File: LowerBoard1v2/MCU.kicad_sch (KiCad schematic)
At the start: 113 parts, among them J401 PWR, J402 DATA, J403 SWD Header, J404 MIDI_In, J405 Micro_SD_Card_Det2, J406 MIDI_Out, J407 MIDI_Thru, J408 POWER, SW401 RST, SW402 BOOT, U401 STM32F411RETx, U402 TPS56528DDA, U404 74HC04, U405 6N138, Y401 16MHz, Y402 32.768kHZ

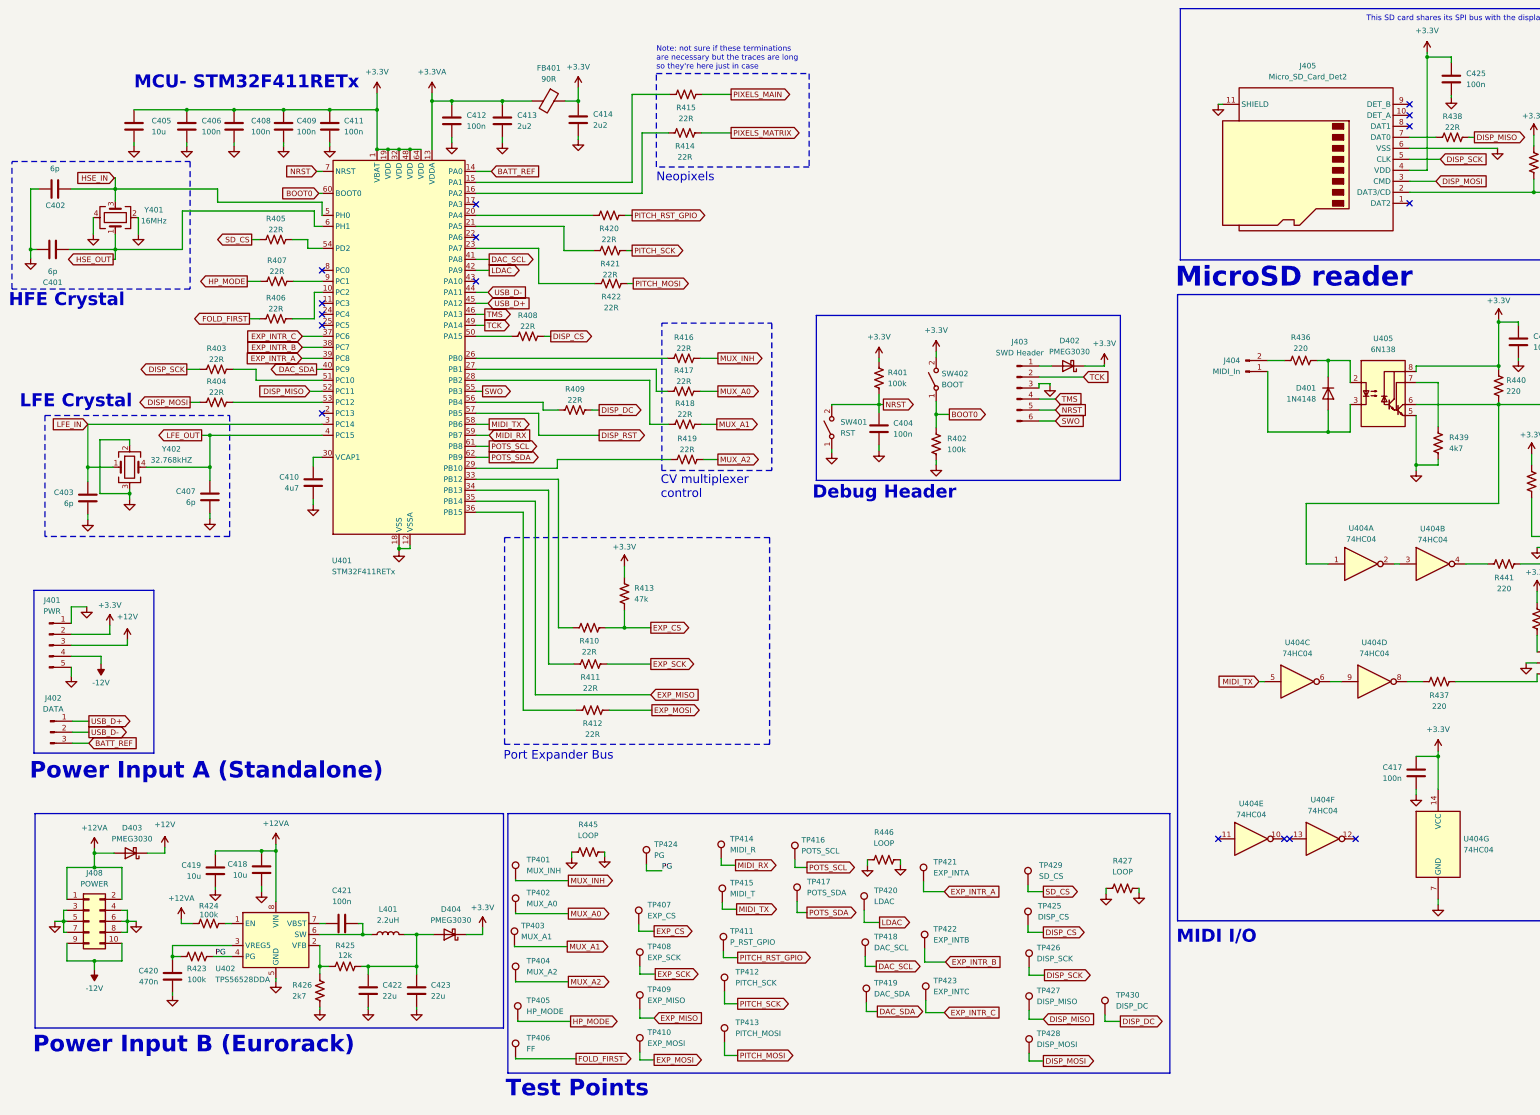
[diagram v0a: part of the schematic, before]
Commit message: switched to resistor arrays for schematic
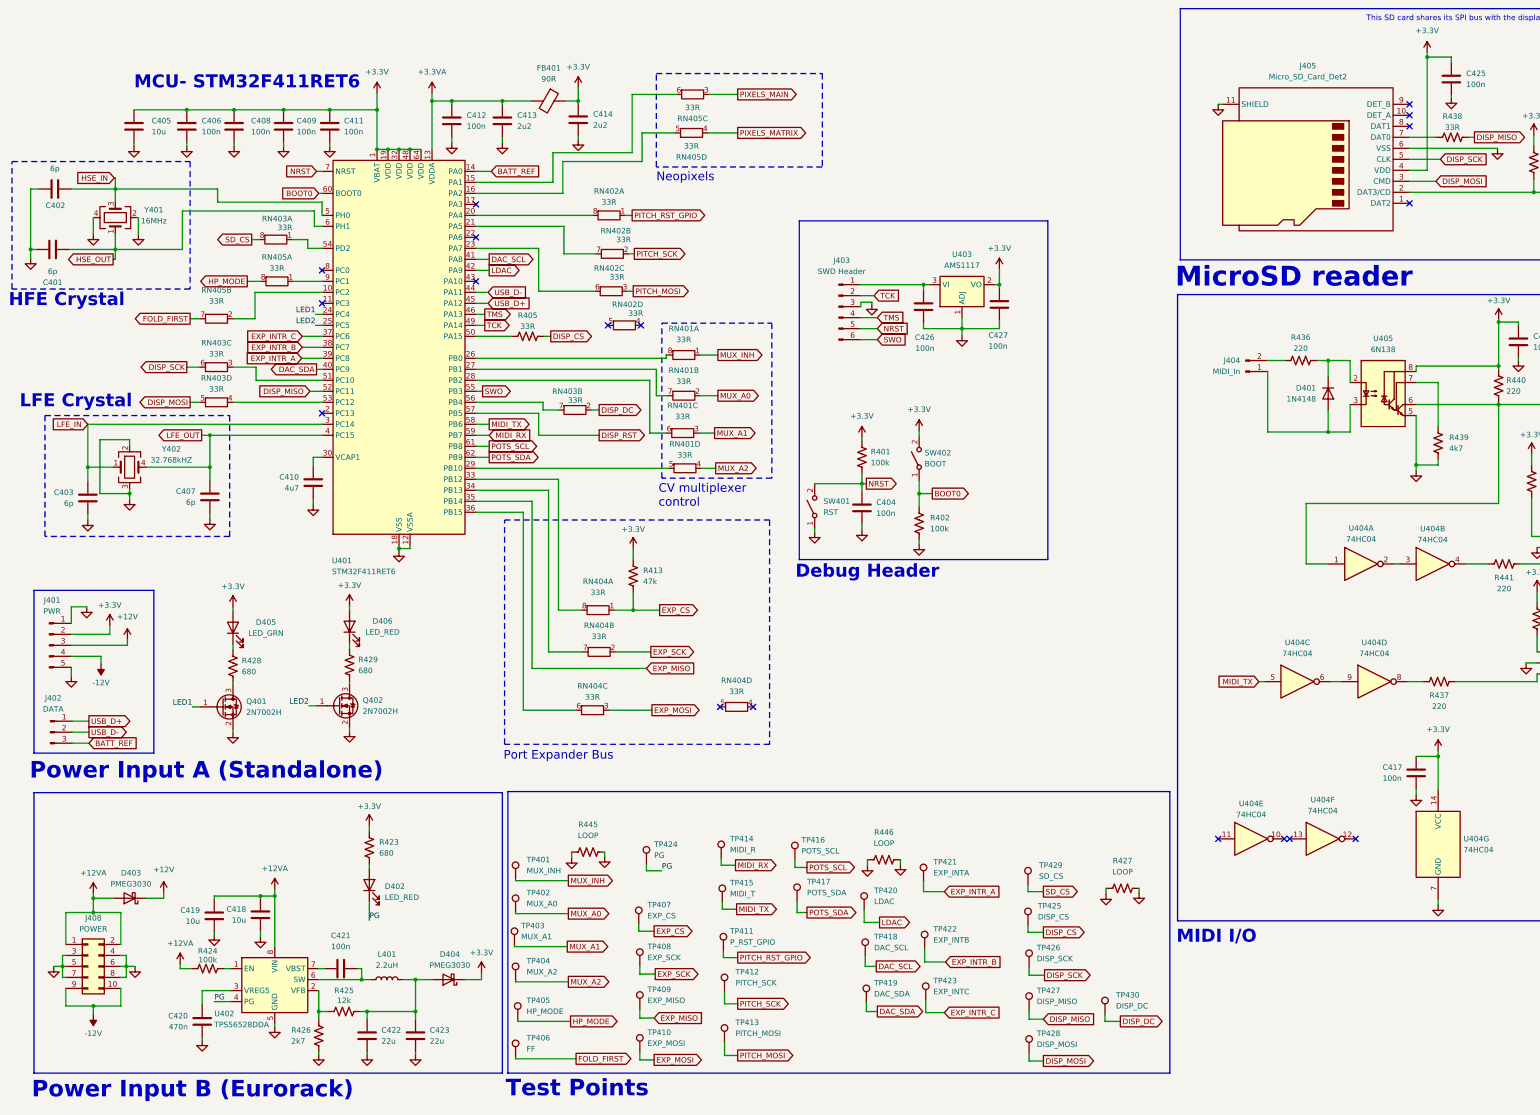
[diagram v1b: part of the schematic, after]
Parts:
- removed D402: PMEG3030, Diode_SMD:D_SOD-123, symbol Device:D_Schottky
- removed R403, R404, R406, R407, R408, R409, R410, R411, R412, R414, R415, R416, R417, R418, R419, R420, R421, R422: 22R, Resistor_SMD:R_0805_2012Metric, symbol Device:R_US
- added C426, C427: 100n, Capacitor_SMD:C_0805_2012Metric, symbol Device:C
- added D402: LED_RED, LED_SMD:LED_0805_2012Metric, symbol Device:LED
- added D405: LED_GRN, LED_THT:LED_D3.0mm, symbol Device:LED
- added D406: LED_RED, LED_THT:LED_D3.0mm, symbol Device:LED
- added Q401, Q402: 2N7002H, Package_TO_SOT_SMD:SOT-23, symbol Transistor_FET:2N7002H
- added R428, R429: 680, Resistor_SMD:R_0805_2012Metric, symbol Device:R_US
- added RN401, RN402, RN403, RN404, RN405: 33R, Resistor_SMD:R_Array_Concave_4x0603, symbol Device:R_Pack04_Split
- added U403: AMS1117, Package_TO_SOT_SMD:SOT-223-3_TabPin2, symbol Regulator_Linear:AMS1117
- R405, R438: value 22R -> 33R
- R423: value 100k -> 680
- U401: value STM32F411RETx -> STM32F411RET6
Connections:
- net +3.3V: now also R423.1, C427.2, D405.2 (A), D406.2 (A), U403.2 (VO)
- net DISP_CS: now also R405.2
- net DISP_DC: now also RN403.2 (R2.1)
- net DISP_MOSI: now also RN403.5 (R4.2)
- net DISP_SCK: now also RN403.6 (R3.2)
- net EXP_CS: now also RN404.1 (R1.1)
- net EXP_MOSI: now also RN404.3 (R3.1)
- net EXP_SCK: now also RN404.2 (R2.1)
- net FOLD_FIRST: now also RN405.7 (R2.2)
- net GND: now also C426.1, C427.1, Q401.2 (S), Q402.2 (S), U403.1 (ADJ)
- net HP_MODE: now also RN405.8 (R1.2)
- net MUX_A0: now also RN401.2 (R2.1)
- net MUX_A1: now also RN401.3 (R3.1)
- net MUX_A2: now also RN401.4 (R4.1)
- net MUX_INH: now also RN401.1 (R1.1)
- net PG: now also D402.1 (K); no longer R423.2
- net PITCH_MOSI: now also RN402.3 (R3.1)
- net PITCH_RST_GPIO: now also RN402.1 (R1.1)
- net PITCH_SCK: now also RN402.2 (R2.1)
- net PIXELS_MAIN: now also RN405.3 (R3.1)
- net PIXELS_MATRIX: now also RN405.4 (R4.1)
- net SD_CS: now also RN403.8 (R1.2); no longer R405.1
- net at U401.34 (PB13): now also RN404.7 (R2.2)
- net at U401.23 (PA7): now also RN402.6 (R3.2)
- net at U401.10 (PC2): now also RN405.2 (R2.1)
- net at U401.36 (PB15): now also RN404.6 (R3.2)
- net at J403.1 (Pin_1): now also C426.2, U403.3 (VI)
- net at U401.15 (PA1): now also RN405.6 (R3.2)
- net at U401.16 (PA2): now also RN405.5 (R4.2)
- net at U401.20 (PA4): now also RN402.8 (R1.2)
- net at U401.21 (PA5): now also RN402.7 (R2.2)
- net LED1: now reaches U401.24 (PC4)
- net LED1: now also Q401.1 (G)
- net LED2: now reaches U401.25 (PC5)
- net LED2: now also Q402.1 (G)
- net at U401.26 (PB0): now also RN401.8 (R1.2)
- net at U401.27 (PB1): now also RN401.7 (R2.2)
- net at U401.28 (PB2): now also RN401.6 (R3.2)
- net at U401.29 (PB10): now also RN401.5 (R4.2)
- net at U401.33 (PB12): now also RN404.8 (R1.2)
- net at U401.50 (PA15): now also R405.1
- net at U401.51 (PC10): now also RN403.3 (R3.1)
- net at U401.53 (PC12): now also RN403.4 (R4.1)
- net at U401.54 (PD2): now also RN403.1 (R1.1); no longer R405.2
- net at U401.56 (PB4): now also RN403.7 (R2.2)
- net at U401.9 (PC1): now also RN405.1 (R1.1)
- net at C420.1, U402.3 (VREG5): no longer R423.1
- new net: Q402.3 (D), R429.2
- new net: D406.1 (K), R429.1
- new net: D402.2 (A), R423.2
- new net: D405.1 (K), R428.1
- new net: Q401.3 (D), R428.2
- no-connect marks 16 -> 18
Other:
- note added: "MCU- STM32F411RET6"
- note removed: "MCU- STM32F411RETx"
- note removed: "Note: not sure if these terminations are necessary but the traces are long so they're here just in case"
- moved on the sheet: C404, C418, C419, C420, C421, C422, C423, D403, D404, J403, J408, L401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

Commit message: 1v2 layout
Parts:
- D405, D406: footprint LED_THT:LED_D3.0mm -> LED_SMD:LED_0805_2012Metric
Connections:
- net DISP_DC: now also RN403.8 (R1.2); no longer RN403.2 (R2.1)
- net DISP_MOSI: now also RN403.6 (R3.2); no longer RN403.5 (R4.2)
- net DISP_SCK: now also RN403.5 (R4.2); no longer RN403.6 (R3.2)
- net FOLD_FIRST: now also RN405.2 (R2.1); no longer RN405.7 (R2.2)
- net HP_MODE: now also RN405.1 (R1.1); no longer RN405.8 (R1.2)
- net SD_CS: now also RN403.7 (R2.2); no longer RN403.8 (R1.2)
- net at RN403.1 (R1.1): now also U401.56 (PB4); no longer U401.54 (PD2)
- net at U401.10 (PC2): now also RN405.7 (R2.2); no longer RN405.2 (R2.1)
- net at U401.51 (PC10): now also RN403.4 (R4.1); no longer RN403.3 (R3.1)
- net at U401.53 (PC12): now also RN403.3 (R3.1); no longer RN403.4 (R4.1)
- net at U401.9 (PC1): now also RN405.8 (R1.2); no longer RN405.1 (R1.1)
- new net: RN403.2 (R2.1), U401.54 (PD2)
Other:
- moved on the sheet: RN403A, RN403B, RN403C, RN403D, RN405A, RN405B
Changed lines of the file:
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@@
 		(exclude_from_sim no)
 		(in_bom no)
-		(on_board yes)
+		(on_board no)
 		(dnp no)
 		(fields_autoplaced yes)
@@
 		(exclude_from_sim no)
 		(in_bom no)
-		(on_board yes)
+		(on_board no)
 		(dnp no)
 		(fields_autoplaced yes)
@@
 		(exclude_from_sim no)
 		(in_bom no)
-		(on_board yes)
+		(on_board no)
 		(dnp no)
 		(fields_autoplaced yes)
@@
 	(symbol
 		(lib_id "Device:R_Pack04_Split")
-		(at 81.534 68.326 90)
+		(at 150.622 107.696 270)
+		(mirror x)
 		(unit 1)
 		(exclude_from_sim no)
@@
 		(dnp no)
 		(property "Reference" "RN403"
-			(at 85.344 64.262 90)
+			(at 146.812 103.632 90)
 			(effects
 				(font
@@
 		)
 		(property "Value" "33R"
-			(at 85.344 66.294 90)
+			(at 146.812 105.664 90)
 			(effects
 				(font
@@
 		)
 		(property "Footprint" "Resistor_SMD:R_Array_Concave_4x0603"
-			(at 81.534 70.358 90)
+			(at 150.622 109.728 90)
 			(effects
 				(font
@@
 		)
 		(property "Datasheet" "~"
-			(at 81.534 68.326 0)
+			(at 150.622 107.696 0)
 			(effects
 				(font
@@
 		)
 		(property "Description" "4 resistor network, parallel topology, split"
-			(at 81.534 68.326 0)
+			(at 150.622 107.696 0)
 			(effects
 				(font
@@
 		(exclude_from_sim no)
 		(in_bom no)
-		(on_board yes)
+		(on_board no)
 		(dnp no)
 		(fields_autoplaced yes)
@@
 		(exclude_from_sim no)
 		(in_bom no)
-		(on_board yes)
+		(on_board no)
 		(dnp no)
 		(fields_autoplaced yes)
@@
 		(exclude_from_sim no)
 		(in_bom no)
-		(on_board yes)
+		(on_board no)
 		(dnp no)
 		(fields_autoplaced yes)
@@
 		(exclude_from_sim no)
 		(in_bom no)
-		(on_board yes)
+		(on_board no)
 		(dnp no)
 		(fields_autoplaced yes)
@@
 		(exclude_from_sim no)
 		(in_bom no)
-		(on_board yes)
+		(on_board no)
 		(dnp no)
 		(fields_autoplaced yes)
@@
 	(symbol
 		(lib_id "Device:R_Pack04_Split")
-		(at 150.622 107.696 90)
+		(at 81.534 68.326 90)
 		(unit 2)
 		(exclude_from_sim no)
@@
 		(dnp no)
 		(property "Reference" "RN403"
-			(at 152.4 104.14 90)
+			(at 83.312 64.77 90)
 			(effects
 				(font
@@
 		)
 		(property "Value" "33R"
-			(at 152.4 106.172 90)
+			(at 83.312 66.802 90)
 			(effects
 				(font
@@
 		)
 		(property "Footprint" "Resistor_SMD:R_Array_Concave_4x0603"
-			(at 150.622 109.728 90)
+			(at 81.534 70.358 90)
 			(effects
 				(font
@@
 		)
 		(property "Datasheet" "~"
-			(at 150.622 107.696 0)
+			(at 81.534 68.326 0)
 			(effects
 				(font
@@
 		)
 		(property "Description" "4 resistor network, parallel topology, split"
-			(at 150.622 107.696 0)
+			(at 81.534 68.326 0)
 			(effects
 				(font
@@
 		(exclude_from_sim no)
 		(in_bom no)
-		(on_board yes)
+		(on_board no)
 		(dnp no)
 		(fields_autoplaced yes)
@@
 		(exclude_from_sim no)
 		(in_bom no)
-		(on_board yes)
+		(on_board no)
 		(dnp no)
 		(fields_autoplaced yes)
@@
 		(exclude_from_sim no)
 		(in_bom no)
-		(on_board yes)
+		(on_board no)
 		(dnp no)
 		(fields_autoplaced yes)
@@
 		(exclude_from_sim no)
 		(in_bom no)
-		(on_board yes)
+		(on_board no)
 		(dnp no)
 		(fields_autoplaced yes)
@@
 		(exclude_from_sim no)
 		(in_bom no)
-		(on_board yes)
+		(on_board no)
 		(dnp no)
 		(fields_autoplaced yes)
@@
 		(exclude_from_sim no)
 		(in_bom no)
-		(on_board yes)
+		(on_board no)
 		(dnp no)
 		(fields_autoplaced yes)
@@
 	(symbol
 		(lib_id "Device:R_Pack04_Split")
-		(at 67.818 105.918 90)
+		(at 67.818 97.79 90)
 		(unit 4)
 		(exclude_from_sim no)
@@
 		(fields_autoplaced yes)
 		(property "Reference" "RN403"
-			(at 67.818 100.33 90)
+			(at 67.818 92.202 90)
 			(effects
 				(font
@@
 		)
 		(property "Value" "33R"
-			(at 67.818 102.87 90)
+			(at 67.818 94.742 90)
 			(effects
 				(font
@@
 		)
 		(property "Footprint" "Resistor_SMD:R_Array_Concave_4x0603"
-			(at 67.818 107.95 90)
+			(at 67.818 99.822 90)
 			(effects
 				(font
@@
 		)
 		(property "Datasheet" "~"
-			(at 67.818 105.918 0)
+			(at 67.818 97.79 0)
 			(effects
 				(font
@@
 		)
 		(property "Description" "4 resistor network, parallel topology, split"
-			(at 67.818 105.918 0)
+			(at 67.818 97.79 0)
 			(effects
 				(font
@@
 		(exclude_from_sim no)
 		(in_bom no)
-		(on_board yes)
+		(on_board no)
 		(dnp no)
 		(fields_autoplaced yes)
@@
 		(exclude_from_sim no)
 		(in_bom no)
-		(on_board yes)
+		(on_board no)
 		(dnp no)
 		(fields_autoplaced yes)
@@
 		(exclude_from_sim no)
 		(in_bom no)
-		(on_board yes)
+		(on_board no)
 		(dnp no)
 		(fields_autoplaced yes)
@@
 	(symbol
 		(lib_id "Device:R_Pack04_Split")
-		(at 67.818 97.79 90)
+		(at 67.818 105.918 90)
 		(unit 3)
 		(exclude_from_sim no)
@@
 		(fields_autoplaced yes)
 		(property "Reference" "RN403"
-			(at 67.818 92.202 90)
+			(at 67.818 100.33 90)
 			(effects
 				(font
@@
 		)
 		(property "Value" "33R"
-			(at 67.818 94.742 90)
+			(at 67.818 102.87 90)
 			(effects
 				(font
@@
 		)
 		(property "Footprint" "Resistor_SMD:R_Array_Concave_4x0603"
-			(at 67.818 99.822 90)
+			(at 67.818 107.95 90)
 			(effects
 				(font
@@
 		)
 		(property "Datasheet" "~"
-			(at 67.818 97.79 0)
+			(at 67.818 105.918 0)
 			(effects
 				(font
@@
 		)
 		(property "Description" "4 resistor network, parallel topology, split"
-			(at 67.818 97.79 0)
+			(at 67.818 105.918 0)
 			(effects
 				(font
@@
 		(exclude_from_sim no)
 		(in_bom no)
-		(on_board yes)
+		(on_board no)
 		(dnp no)
 		(fields_autoplaced yes)
@@
 		(exclude_from_sim no)
 		(in_bom no)
-		(on_board yes)
+		(on_board no)
 		(dnp no)
 		(fields_autoplaced yes)
@@
 		(exclude_from_sim no)
 		(in_bom no)
-		(on_board yes)
+		(on_board no)
 		(dnp no)
 		(fields_autoplaced yes)
@@
 		(exclude_from_sim no)
 		(in_bom no)
-		(on_board yes)
+		(on_board no)
 		(dnp no)
 		(fields_autoplaced yes)
@@
 	(symbol
 		(lib_id "Device:R_Pack04_Split")
-		(at 81.788 77.978 90)
+		(at 81.788 77.978 270)
+		(mirror x)
 		(unit 1)
 		(exclude_from_sim no)
@@
 		(on_board yes)
 		(dnp no)
-		(fields_autoplaced yes)
 		(property "Reference" "RN405"
 			(at 81.788 72.39 90)
@@
 		(exclude_from_sim no)
 		(in_bom no)
-		(on_board yes)
+		(on_board no)
 		(dnp no)
 		(fields_autoplaced yes)
@@
 		(exclude_from_sim no)
 		(in_bom no)
-		(on_board yes)
+		(on_board no)
 		(dnp no)
 		(fields_autoplaced yes)
@@
 	(symbol
 		(lib_id "Device:R_Pack04_Split")
-		(at 67.818 86.614 90)
+		(at 67.818 86.614 270)
+		(mirror x)
 		(unit 2)
 		(exclude_from_sim no)
@@
 		(on_board yes)
 		(dnp no)
-		(fields_autoplaced yes)
 		(property "Reference" "RN405"
-			(at 67.818 80.01 90)
+			(at 67.818 81.026 90)
 			(effects
 				(font
@@
 		)
 		(property "Value" "33R"
-			(at 67.818 82.55 90)
+			(at 67.818 83.566 90)
 			(effects
 				(font
@@
 		(exclude_from_sim no)
 		(in_bom no)
-		(on_board yes)
+		(on_board no)
 		(dnp no)
 		(fields_autoplaced yes)
@@
 			)
 		)
-		(property "Footprint" "LED_THT:LED_D3.0mm"
+		(property "Footprint" "LED_SMD:LED_0805_2012Metric"
 			(at 71.628 157.988 0)
 			(effects
@@
 		(exclude_from_sim no)
 		(in_bom no)
-		(on_board yes)
+		(on_board no)
 		(dnp no)
 		(fields_autoplaced yes)
@@
 		(exclude_from_sim no)
 		(in_bom no)
-		(on_board yes)
+		(on_board no)
 		(dnp no)
 		(fields_autoplaced yes)
@@
 		(exclude_from_sim no)
 		(in_bom no)
-		(on_board yes)
+		(on_board no)
 		(dnp no)
 		(fields_autoplaced yes)
@@
 		(exclude_from_sim no)
 		(in_bom no)
-		(on_board yes)
+		(on_board no)
 		(dnp no)
 		(fields_autoplaced yes)
@@
 			)
 		)
-		(property "Footprint" "LED_THT:LED_D3.0mm"
+		(property "Footprint" "LED_SMD:LED_0805_2012Metric"
 			(at 98.552 157.734 0)
 			(effects
@@
 		(exclude_from_sim no)
 		(in_bom no)
-		(on_board yes)
+		(on_board no)
 		(dnp no)
 		(fields_autoplaced yes)
@@
 		(exclude_from_sim no)
 		(in_bom no)
-		(on_board yes)
+		(on_board no)
 		(dnp no)
 		(fields_autoplaced yes)

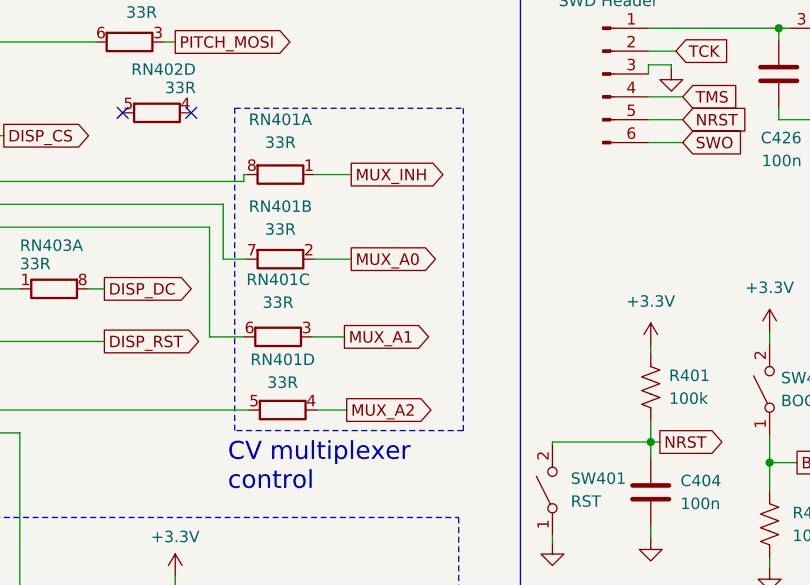
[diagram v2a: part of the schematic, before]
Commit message: simplified voice clock a bit
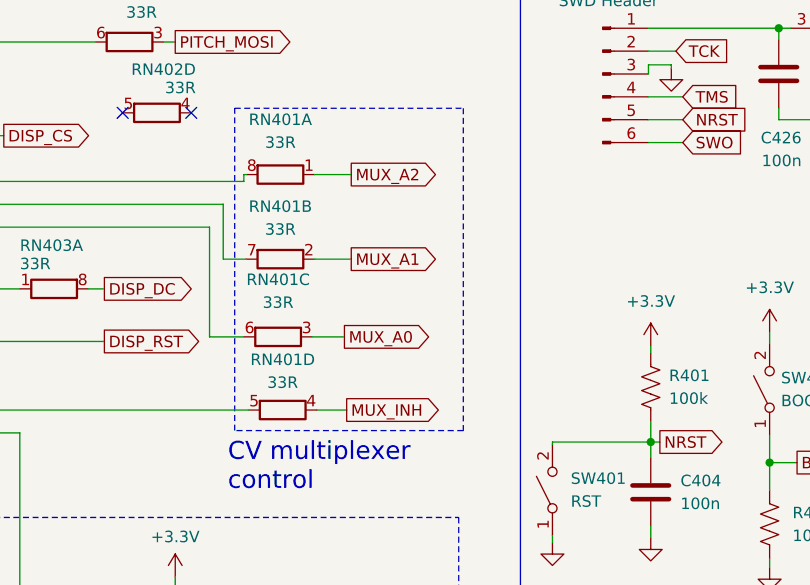
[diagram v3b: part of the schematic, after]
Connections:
- net MUX_A0: now also RN401.3 (R3.1); no longer RN401.2 (R2.1)
- net MUX_A1: now also RN401.2 (R2.1); no longer RN401.3 (R3.1)
- net MUX_A2: now also RN401.1 (R1.1); no longer RN401.4 (R4.1)
- net MUX_INH: now also RN401.4 (R4.1); no longer RN401.1 (R1.1)
